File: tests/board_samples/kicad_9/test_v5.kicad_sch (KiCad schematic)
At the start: 4 parts

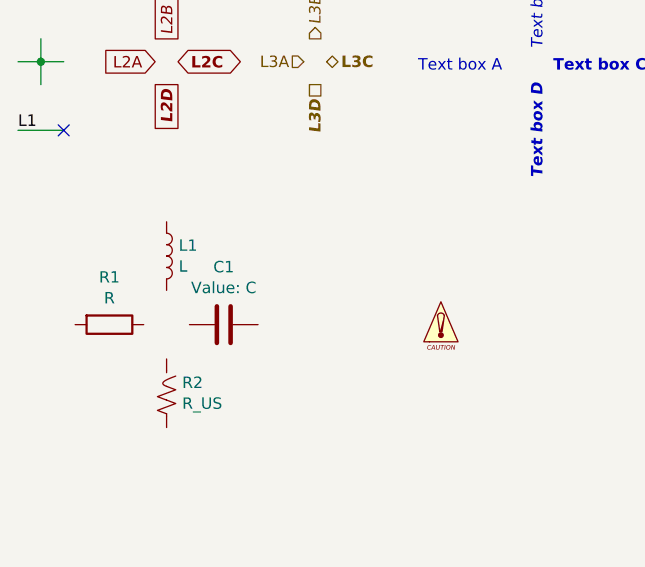
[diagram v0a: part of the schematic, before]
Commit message: [Schematic][Added] Support for private fields
Closes #812
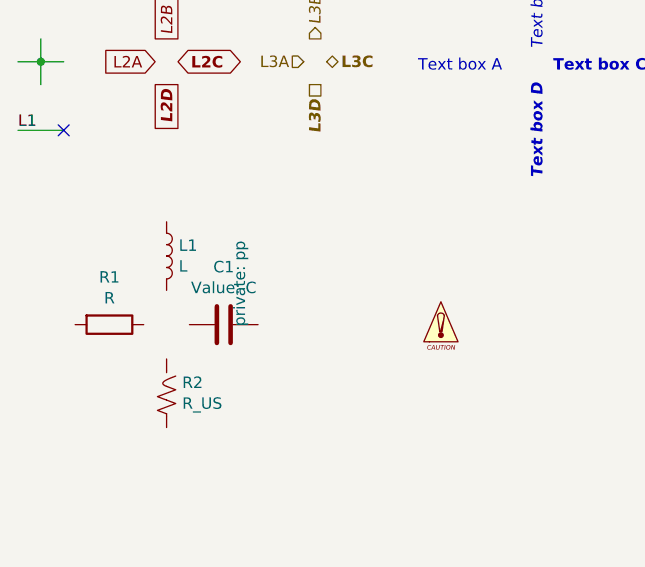
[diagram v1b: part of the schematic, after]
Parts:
- C1: private (none) -> pp
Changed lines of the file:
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@@
 (kicad_sch
-	(version 20241209)
+	(version 20250114)
 	(generator "eeschema")
 	(generator_version "9.0")
@@
 			"TBljjJUZEviqLuceLPU4GGNsO1pXc9LWg490w8T/BtC4weNhjDG2ucYhxG8MvPqlfyj1QBhjbLta"
 			"92oBndf/RjgD9QEIvA3A2wB0bNioGGOMFZG4AKIfQeDHKmW+fuH150ZLPSLGGNvONmb5LgDhA4/U"
-			"q4a8TpG0ZElYxhhjpWeYwsgo5pnRV58dK/VYGGOMXfX/ARD6Y1WuLYYhAAAAAElFTkSuQmCC"
+			"q4a8TpG0ZElYxhhjpWeYwsgo5pnRV58dK/VYGGOMXfX/ARD6Y1WuLYYhAAAAAElFTkSuQmCCAAAA"
+			"AAAAAAAAAAAAAAAAAAAAAAAAAAAAAAAAAAAAAAAAAAAAAAAAAAAAAAAAAAAAAAAAAAAAAAAAAAAA"
+			"AAAAAAAAAAAAAAAAAAAAAAAAAAAAAAAAAAAAAAAAAAAAAAAAAAAAAAAAAAAAAAAAAAAAAAAAAAAA"
+			"AAAAAAAAAAAAAAAAAAAAAAAAAAAAAAAAAAAAAAAAAAAAAAAAAAAAAAAAAAAAAAAAAAAAAAAAAAAA"
+			"AAAAAAAAAAAAAAAAAAAAAAAAAAAAAAAAAAAAAAAAAAAAAAAAAAAAAAAAAAAAAAAAAAAAAAAAAAAA"
+			"AAAAAAAAAAAAAAAAAAAAAAAAAAAAAAAAAAAAAAAAAAAAAAAAAAAAAAAAAAAAAAAAAAAAAAAAAAAA"
+			"AAAAAAAAAAAAAAAAAAAAAAAAAAAAAAAAAAAAAAAAAAAAAAAAAAAAAAAAAAAAAAAAAAAAAAAAAAAA"
+			"AAAAAAAAAAAAAAAAAAAAAAAAAAAAAAAAAAAAAAAAAAAAAAAAAAAAAAAAAAAAAAAAAAAAAAAAAAAA"
+			"AAAAAAAAAAAAAAAAAAAAAAAAAAAAAAAAAAAAAAAAAAAAAAAAAAAAAAAAAAAAAAAAAAAAAAAAAAAA"
+			"AAAAAAAAAAAAAAAAAAAAAAAAAAAAAAAAAAAAAAAAAAAAAAAAAAAAAAAAAAAAAAAAAAAAAAAAAAAA"
+			"AAAAAAAAAAAAAAAAAAAAAAAAAAAAAAAAAAAAAAAAAAAAAAAAAAAAAAAAAAAAAAAAAAAAAAAAAAAA"
+			"AAAAAAAAAAAAAAAAAAAAAAAAAAAAAAAAAAAAAAAAAAAAAAAAAAAAAAAAAAAAAAAAAAAAAAAAAAAA"
+			"AAAAAAAAAAAAAAAAAAAAAAAAAAAAAAAAAAAAAAAAAAAAAAAAAAAAAAAAAAAAAAAAAAAAAAAAAAAA"
+			"AAAAAAAAAAAAAAAAAAAAAAAAAAAAAAAAAAAAAAAAAAAAAAAAAAAAAAAAAAAAAAAAAAAAAAAAAAAA"
+			"AAAAAAAAAAAAAAAAAAAAAAAAAAAAAAAAAAAAAAAAAAAAAAAAAAAAAAAAAAAAAAAAAAAAAAAAAAAA"
+			"AAAAAAAAAAAAAAAAAAAAAAAAAAAAAAAAAAAAAAAAAAAAAAAAAAAAAAAAAAAAAAAAAAAAAAAAAAAA"
+			"AAAAAAAAAAAAAAAAAAAAAAAAAAAAAAAAAAAAAAAAAAAAAAAAAAAAAAAAAAAAAAAAAAAAAAAAAAAA"
+			"AAAAAAAAAAAAAAAAAAAAAAAAAAAAAAAAAAAAAAAAAAAAAAAAAAAAAAAAAAAAAAAAAAAAAAAAAAAA"
+			"AAAAAAAAAAAAAAAAAAAAAAAAAAAAAAAAAAAAAAAAAAAAAAAAAAAAAAAAAAAAAAAAAAAAAA=="
 		)
 	)
@@
 			)
 		)
+		(property private "pp" ""
+			(at 47.498 83.058 0)
+			(show_name yes)
+			(effects
+				(font
+					(size 1.27 1.27)
+				)
+			)
+		)
